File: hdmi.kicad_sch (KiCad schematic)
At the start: 41 parts, among them J13 HDMI-Mini-C_WE_685119136923, Q12 PJE138K, Q2 PJE138K, U43 NTS0102_XSON, U44 TPD4E05U06QDQARQ1, U45 TPD4E05U06QDQARQ1, U46 TPD4E05U06QDQARQ1

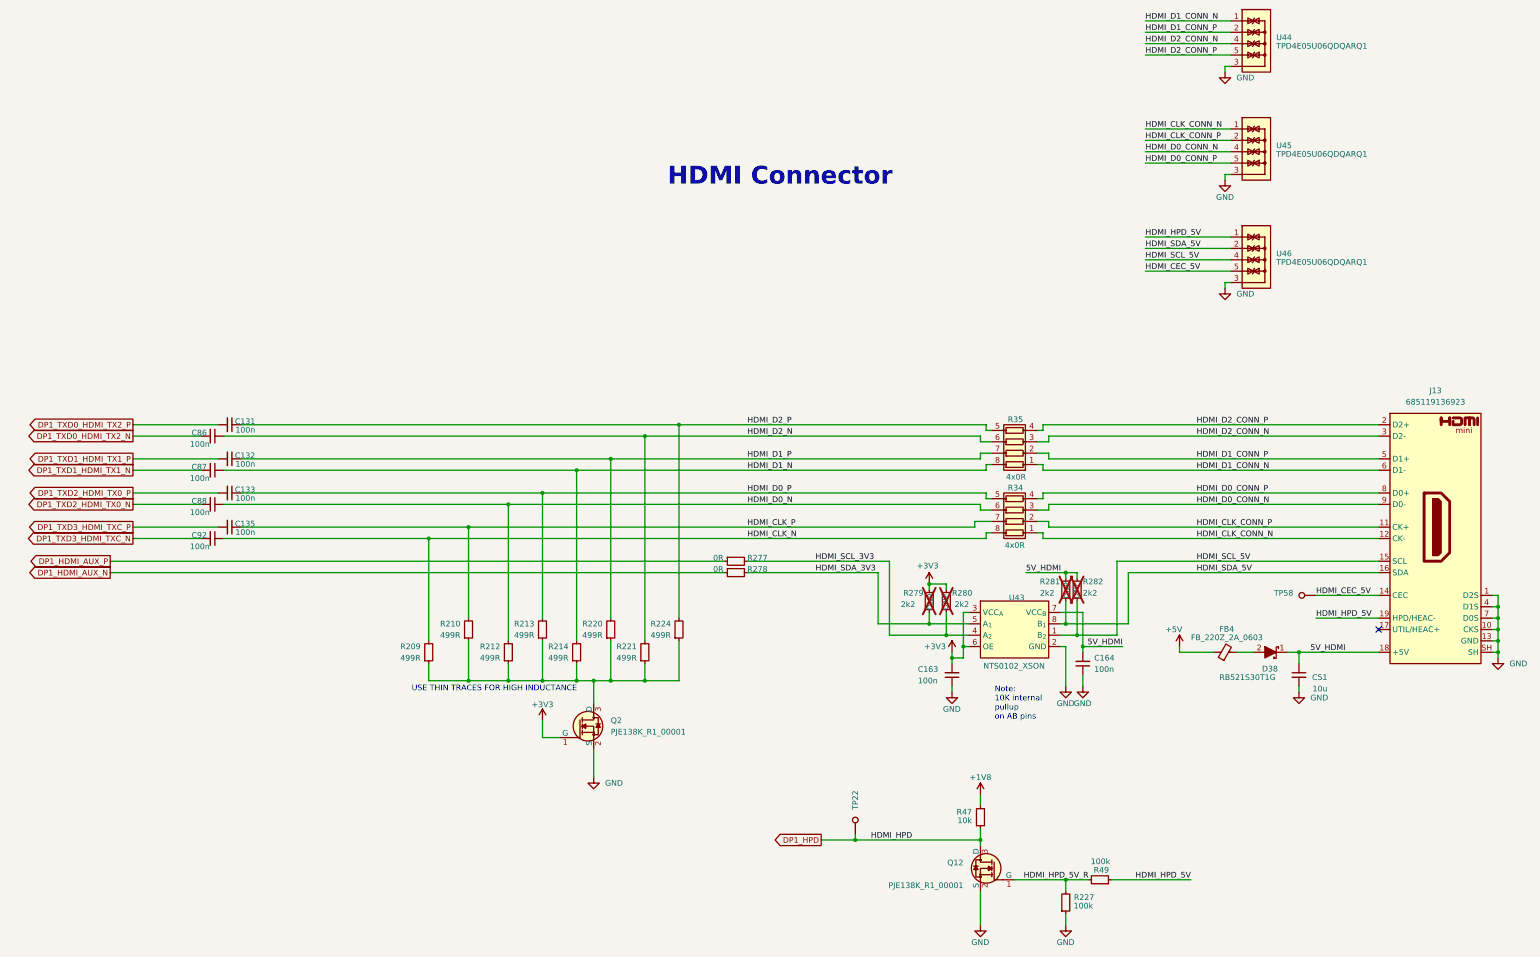
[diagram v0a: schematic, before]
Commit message: Schematic Cleanup, Complete routing
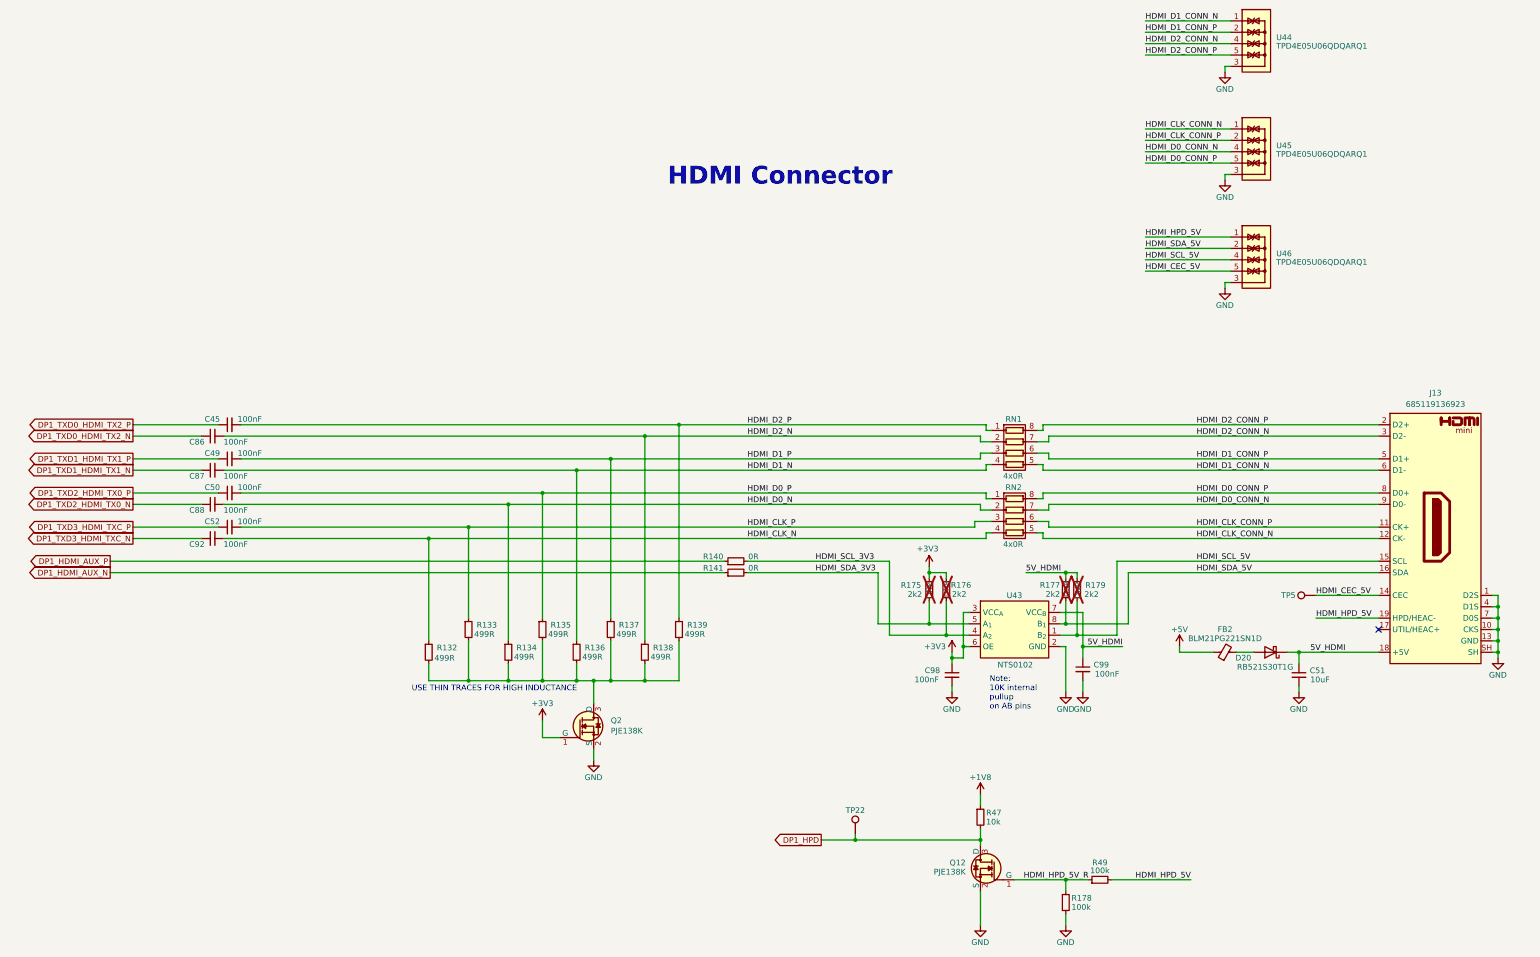
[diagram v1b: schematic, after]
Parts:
- C45: renamed from C131; value C_100n_0402 -> 100nF; symbol antmicroCapacitors0402:C_100n_0402 -> Device:C_Small
- C49: renamed from C132; value C_100n_0402 -> 100nF; symbol antmicroCapacitors0402:C_100n_0402 -> Device:C_Small
- C50: renamed from C133; value C_100n_0402 -> 100nF; symbol antmicroCapacitors0402:C_100n_0402 -> Device:C_Small
- C51: value C_10u_0603 -> 10uF; symbol antmicroCapacitors0603:C_10u_0603 -> Device:C_Small
- C52: renamed from C135; value C_100n_0402 -> 100nF; symbol antmicroCapacitors0402:C_100n_0402 -> Device:C_Small
- C86, C87, C88, C92: value C_100n_0402 -> 100nF; symbol antmicroCapacitors0402:C_100n_0402 -> Device:C_Small
- C98: renamed from C163; value C_100n_0603 -> 100nF; symbol antmicroCapacitors0402:C_100n_0402 -> Device:C_Small
- C99: renamed from C164; value C_100n_0603 -> 100nF; symbol antmicroCapacitors0402:C_100n_0402 -> Device:C_Small
- D20: renamed from D38; symbol antmicroDiodesRectifiersSingle:RB521S30T1G -> Device:D_Schottky
- FB2: renamed from FB4; value FB_220Z_2A_0603 -> BLM21PG221SN1D; symbol antmicroFerriteBeadsandChips:FB_220Z_2A_Murata-BLM21PG_0805 -> Device:FerriteBead_Small
- J13: value HDMI-Mini-C_WE_685119136923 -> 685119136923; symbol antmicroVideoConnectors:HDMI-Mini-C_WE_685119136923 -> JetsonCarrier:HDMI-Mini-C_WE_685119136923
- Q12: symbol antmicroTransistorsFETsMOSFETsSingle:PJE138K -> JetsonCarrier:PJE138K; now in the parts list
- Q2: symbol antmicroTransistorsFETsMOSFETsSingle:PJE138K -> JetsonCarrier:PJE138K
- R132: renamed from R209; value R_499R_0402 -> 499R; symbol antmicroResistors0402:R_499R_0402 -> Device:R_Small
- R133: renamed from R210; value R_499R_0402 -> 499R; symbol antmicroResistors0402:R_499R_0402 -> Device:R_Small
- R134: renamed from R212; value R_499R_0402 -> 499R; symbol antmicroResistors0402:R_499R_0402 -> Device:R_Small
- R135: renamed from R213; value R_499R_0402 -> 499R; symbol antmicroResistors0402:R_499R_0402 -> Device:R_Small
- R136: renamed from R214; value R_499R_0402 -> 499R; symbol antmicroResistors0402:R_499R_0402 -> Device:R_Small
- R137: renamed from R220; value R_499R_0402 -> 499R; symbol antmicroResistors0402:R_499R_0402 -> Device:R_Small
- R138: renamed from R221; value R_499R_0402 -> 499R; symbol antmicroResistors0402:R_499R_0402 -> Device:R_Small
- R139: renamed from R224; value R_499R_0402 -> 499R; symbol antmicroResistors0402:R_499R_0402 -> Device:R_Small
- R140: renamed from R277; value R_0R_0402 -> 0R; symbol antmicroResistors0402:R_0R_0402 -> Device:R_Small
- R141: renamed from R278; value R_0R_0402 -> 0R; symbol antmicroResistors0402:R_0R_0402 -> Device:R_Small
- R175: renamed from R279; value R_2k2_0402 -> 2k2; symbol antmicroResistors0402:R_2k2_0402 -> Device:R_Small; now in the parts list
- R176: renamed from R280; value R_2k2_0402 -> 2k2; symbol antmicroResistors0402:R_2k2_0402 -> Device:R_Small; now in the parts list
- R177: renamed from R281; value R_2k2_0402 -> 2k2; symbol antmicroResistors0402:R_2k2_0402 -> Device:R_Small; now in the parts list
- R178: renamed from R227; value R_100k_0603 -> 100k; symbol antmicroResistors0402:R_2k2_0402 -> Device:R_Small
- R179: renamed from R282; value R_2k2_0402 -> 2k2; symbol antmicroResistors0402:R_2k2_0402 -> Device:R_Small; now in the parts list
- R47: value R_10k_0603 -> 10k; symbol antmicroResistors0402:R_10k_0402 -> Device:R_Small
- R49: value R_100k_0603 -> 100k; symbol antmicroResistors0402:R_2k2_0402 -> Device:R_Small
- RN1: renamed from R35; value R_4x0R_0402_array -> 4x0R; symbol antmicroResistorNetworksArrays:R_4x0R_0201_array -> Device:R_Pack04
- RN2: renamed from R34; value R_4x0R_0402_array -> 4x0R; symbol antmicroResistorNetworksArrays:R_4x0R_0201_array -> Device:R_Pack04
- TP22: symbol antmicroTestPoints:TP_0.75mm_SMD -> Connector:TestPoint
- TP5: renamed from TP58; symbol antmicroTestPoints:TP_0.75mm_SMD -> Connector:TestPoint
- U43: value NTS0102_XSON -> NTS0102; symbol antmicroLogicTranslatorsLevelShifters:NTS0102_XSON -> JetsonCarrier:NTS0102
- U44, U45, U46: symbol antmicroTVSDiodes:TPD4E05U06QDQARQ1 -> JetsonCarrier:TPD4E05U06QDQARQ1
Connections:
- net +1V8: now also R47.1; no longer R47.2
- net +3V3: now also C98.1, R175.1; no longer C98.2, R175.2
- net 5V_HDMI: now also C99.1, R179.1; no longer C99.2, R179.2
- net DP1_HPD: now also R47.2; no longer R47.1
- net DP1_TXD0_HDMI_TX2_N: now also C86.1; no longer C86.2
- net DP1_TXD0_HDMI_TX2_P: now also C45.1; no longer C45.2
- net DP1_TXD1_HDMI_TX1_N: now also C87.1; no longer C87.2
- net DP1_TXD1_HDMI_TX1_P: now also C49.1; no longer C49.2
- net DP1_TXD2_HDMI_TX0_N: now also C88.1; no longer C88.2
- net DP1_TXD2_HDMI_TX0_P: now also C50.1; no longer C50.2
- net DP1_TXD3_HDMI_TXC_N: now also C92.1; no longer C92.2
- net DP1_TXD3_HDMI_TXC_P: now also C52.1; no longer C52.2
- net GND: now also C98.2, C99.2, R178.2; no longer C98.1, C99.1, R178.1
- net HDMI_CLK_CONN_N: now also RN2.5 (R4.2); no longer RN2.1 (R1.1)
- net HDMI_CLK_CONN_P: now also RN2.6 (R3.2); no longer RN2.2 (R2.1)
- net HDMI_CLK_N: now also C92.2, R132.1, RN2.4 (R4.1); no longer C92.1, R132.2, RN2.8 (R1.2)
- net HDMI_CLK_P: now also C52.2, R133.1, RN2.3 (R3.1); no longer C52.1, R133.2, RN2.7 (R2.2)
- net HDMI_D0_CONN_N: now also RN2.7 (R2.2); no longer RN2.3 (R3.1)
- net HDMI_D0_CONN_P: now also RN2.8 (R1.2); no longer RN2.4 (R4.1)
- net HDMI_D0_N: now also C88.2, R134.1, RN2.2 (R2.1); no longer C88.1, R134.2, RN2.6 (R3.2)
- net HDMI_D0_P: now also C50.2, R135.1, RN2.1 (R1.1); no longer C50.1, R135.2, RN2.5 (R4.2)
- net HDMI_D1_CONN_N: now also RN1.5 (R4.2); no longer RN1.1 (R1.1)
- net HDMI_D1_CONN_P: now also RN1.6 (R3.2); no longer RN1.2 (R2.1)
- net HDMI_D1_N: now also C87.2, R136.1, RN1.4 (R4.1); no longer C87.1, R136.2, RN1.8 (R1.2)
- net HDMI_D1_P: now also C49.2, R137.1, RN1.3 (R3.1); no longer C49.1, R137.2, RN1.7 (R2.2)
- net HDMI_D2_CONN_N: now also RN1.7 (R2.2); no longer RN1.3 (R3.1)
- net HDMI_D2_CONN_P: now also RN1.8 (R1.2); no longer RN1.4 (R4.1)
- net HDMI_D2_N: now also C86.2, R138.1, RN1.2 (R2.1); no longer C86.1, R138.2, RN1.6 (R3.2)
- net HDMI_D2_P: now also C45.2, R139.1, RN1.1 (R1.1); no longer C45.1, R139.2, RN1.5 (R4.2)
- net HDMI_HPD_5V: now also R49.2; no longer R49.1
- net HDMI_HPD_5V_R: now also R178.1, R49.1; no longer R178.2, R49.2
- net HDMI_SCL_5V: now also R179.2; no longer R179.1
- net HDMI_SDA_3V3: now also R175.2; no longer R175.1
- new net: Q2.3 (D), R132.2, R133.2, R134.2, R135.2, R136.2, R137.2, R138.2, R139.2
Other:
- moved on the sheet: C45, C49, C50, C51, C52, C86, C87, C88, C92, C98, C99, FB2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
